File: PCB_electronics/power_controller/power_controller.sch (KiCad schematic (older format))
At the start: 20 parts, among them IC1 ATMEGA328-P, P1 SOLAR_PANEL, P2 5V_pololu, P3 BATT, P4 SUPERCAPS, P5 PWR_MEGA, P6 FEEDBACK_MEGA, U1 IRLB-8721_SOL, U2 IRLB-8721_MEGA, Y1 16MHz

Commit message: first version of power controller
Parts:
- IC1: footprint Housings_DIP:DIP-28_W15.24mm_LongPads -> Housings_DIP:DIP-28_W7.62mm_LongPads
- R1, R2, R3, R4, R5, R6, R7: footprint Resistors_ThroughHole:Resistor_Horizontal_RM20mm -> Resistors_ThroughHole:Resistor_Horizontal_RM10mm
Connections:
- net +5V: no longer IC1.21 (AREF)
- no-connect marks 14 -> 15

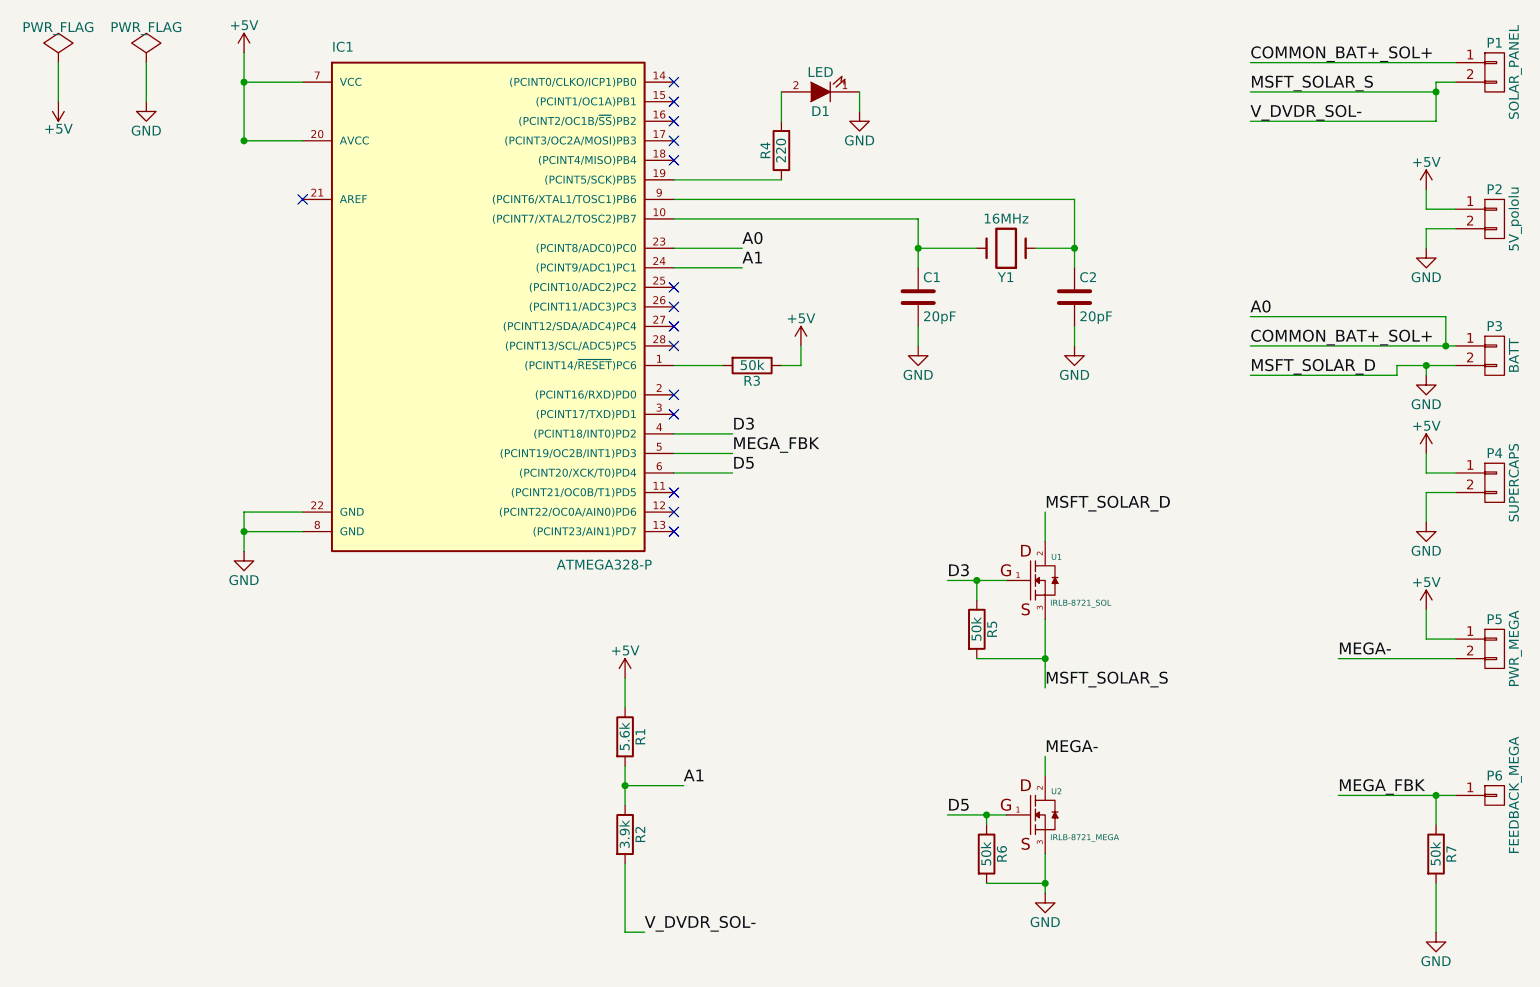
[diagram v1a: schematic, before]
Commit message: correct new PSB with net-tie on master
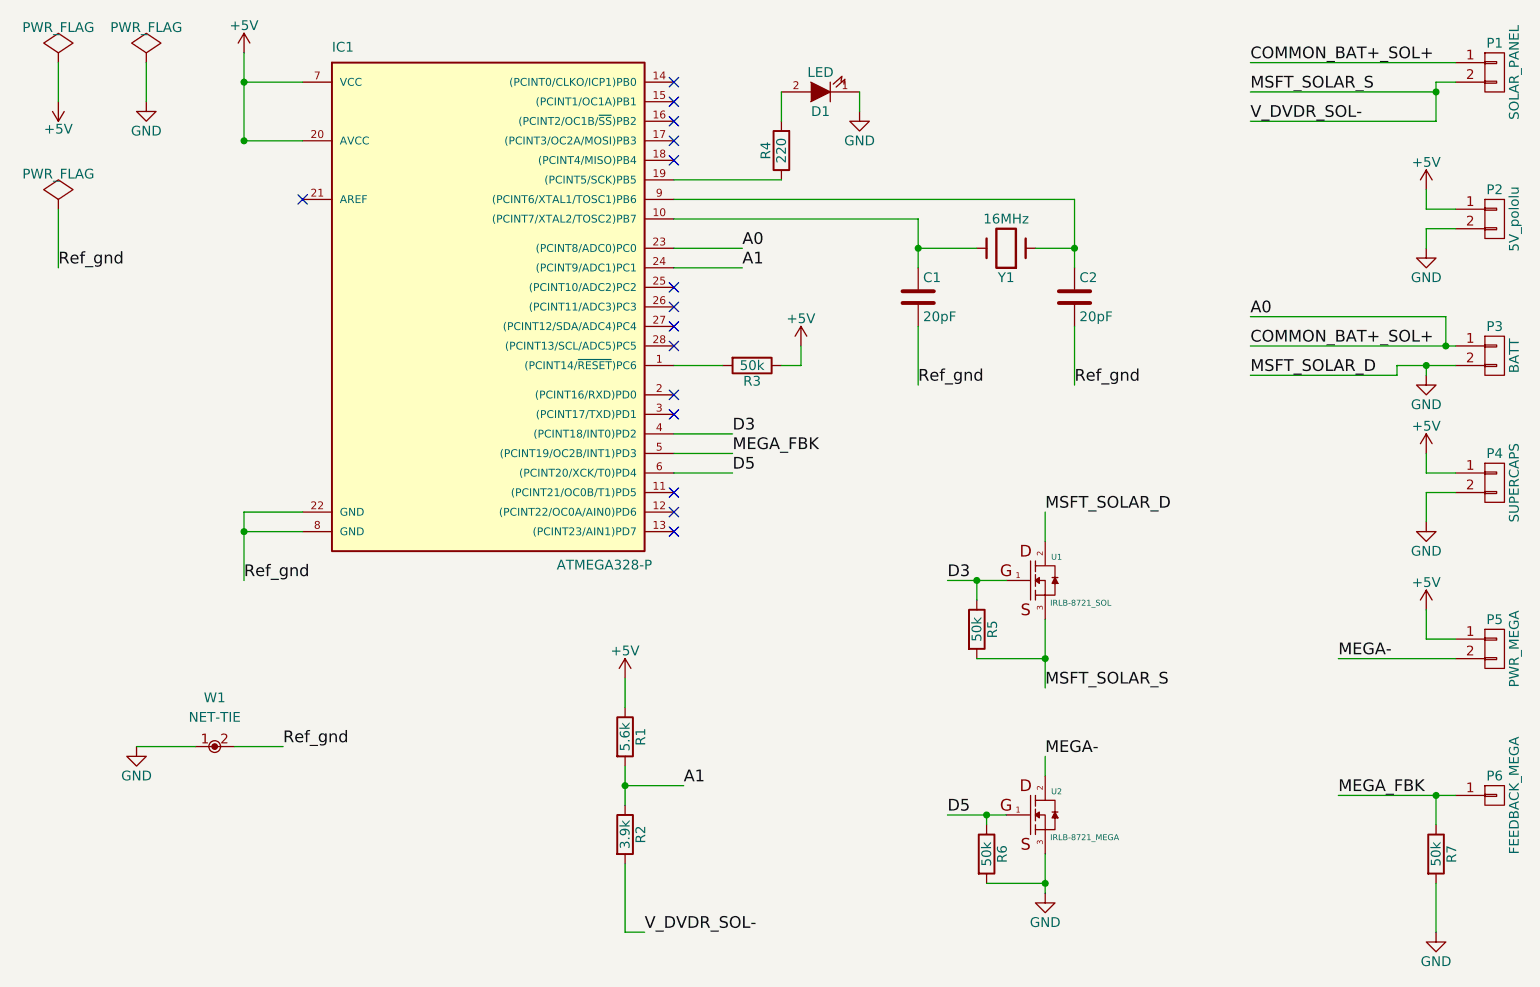
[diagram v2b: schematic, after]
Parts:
- added W1: NET-TIE, conn-test:NET-TIE, symbol NET-TIE
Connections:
- net GND: now also W1.1; no longer C1.2, C2.2, IC1.22 (GND), IC1.8 (GND)
- new net Ref_gnd: C1.2, C2.2, IC1.22 (GND), IC1.8 (GND), W1.2
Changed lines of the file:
@@
 LIBS:MOSFET-P
 LIBS:MOSFET-N
+LIBS:net-tie
 LIBS:power_controller-cache
 EELAYER 25 0
@@
 $EndComp
 $Comp
-L GND #PWR8
-U 1 1 5A1C2D72
-P 5200 3050
-F 0 "#PWR8" H 5200 2800 50  0001 C CNN
-F 1 "GND" H 5200 2900 50  0000 C CNN
-F 2 "" H 5200 3050 50  0000 C CNN
-F 3 "" H 5200 3050 50  0000 C CNN
-	1    5200 3050
-	1    0    0    -1
-$EndComp
-$Comp
-L GND #PWR10
-U 1 1 5A1C2D8E
-P 6000 3050
-F 0 "#PWR10" H 6000 2800 50  0001 C CNN
-F 1 "GND" H 6000 2900 50  0000 C CNN
-F 2 "" H 6000 3050 50  0000 C CNN
-F 3 "" H 6000 3050 50  0000 C CNN
-	1    6000 3050
-	1    0    0    -1
-$EndComp
-$Comp
-L GND #PWR4
-U 1 1 5A1C2E28
-P 1750 4100
-F 0 "#PWR4" H 1750 3850 50  0001 C CNN
-F 1 "GND" H 1750 3950 50  0000 C CNN
-F 2 "" H 1750 4100 50  0000 C CNN
-F 3 "" H 1750 4100 50  0000 C CNN
-	1    1750 4100
-	1    0    0    -1
-$EndComp
-$Comp
-L +5V #PWR3
+L +5V #PWR01
 U 1 1 5A1C2ED1
 P 1750 1550
-F 0 "#PWR3" H 1750 1400 50  0001 C CNN
+F 0 "#PWR01" H 1750 1400 50  0001 C CNN
 F 1 "+5V" H 1750 1690 50  0000 C CNN
 F 2 "" H 1750 1550 50  0000 C CNN
@@
 $EndComp
 $Comp
-L GND #PWR12
+L GND #PWR02
 U 1 1 5A1C31B8
 P 7800 2550
-F 0 "#PWR12" H 7800 2300 50  0001 C CNN
+F 0 "#PWR02" H 7800 2300 50  0001 C CNN
 F 1 "GND" H 7800 2400 50  0000 C CNN
 F 2 "" H 7800 2550 50  0000 C CNN
@@
 $EndComp
 $Comp
-L +5V #PWR11
+L +5V #PWR03
 U 1 1 5A1C322F
 P 7800 2250
-F 0 "#PWR11" H 7800 2100 50  0001 C CNN
+F 0 "#PWR03" H 7800 2100 50  0001 C CNN
 F 1 "+5V" H 7800 2390 50  0000 C CNN
 F 2 "" H 7800 2250 50  0000 C CNN
@@
 $EndComp
 $Comp
-L +5V #PWR14
+L +5V #PWR04
 U 1 1 5A1C3274
 P 7800 3600
-F 0 "#PWR14" H 7800 3450 50  0001 C CNN
+F 0 "#PWR04" H 7800 3450 50  0001 C CNN
 F 1 "+5V" H 7800 3740 50  0000 C CNN
 F 2 "" H 7800 3600 50  0000 C CNN
@@
 $EndComp
 $Comp
-L GND #PWR15
+L GND #PWR05
 U 1 1 5A1C3298
 P 7800 3950
-F 0 "#PWR15" H 7800 3700 50  0001 C CNN
+F 0 "#PWR05" H 7800 3700 50  0001 C CNN
 F 1 "GND" H 7800 3800 50  0000 C CNN
 F 2 "" H 7800 3950 50  0000 C CNN
@@
 A0
 $Comp
-L GND #PWR13
+L GND #PWR06
 U 1 1 5A1C3813
 P 7800 3200
-F 0 "#PWR13" H 7800 2950 50  0001 C CNN
+F 0 "#PWR06" H 7800 2950 50  0001 C CNN
 F 1 "GND" H 7800 3050 50  0000 C CNN
 F 2 "" H 7800 3200 50  0000 C CNN
@@
 $EndComp
 $Comp
-L +5V #PWR6
+L +5V #PWR07
 U 1 1 5A1C3B75
 P 4600 3050
-F 0 "#PWR6" H 4600 2900 50  0001 C CNN
+F 0 "#PWR07" H 4600 2900 50  0001 C CNN
 F 1 "+5V" H 4600 3190 50  0000 C CNN
 F 2 "" H 4600 3050 50  0000 C CNN
@@
 $EndComp
 $Comp
-L +5V #PWR16
+L +5V #PWR08
 U 1 1 5A1C4CA7
 P 7800 4400
-F 0 "#PWR16" H 7800 4250 50  0001 C CNN
+F 0 "#PWR08" H 7800 4250 50  0001 C CNN
 F 1 "+5V" H 7800 4540 50  0000 C CNN
 F 2 "" H 7800 4400 50  0000 C CNN
@@
 D5
 $Comp
-L GND #PWR9
+L GND #PWR09
 U 1 1 5A1C4F56
 P 5850 5850
-F 0 "#PWR9" H 5850 5600 50  0001 C CNN
+F 0 "#PWR09" H 5850 5600 50  0001 C CNN
 F 1 "GND" H 5850 5700 50  0000 C CNN
 F 2 "" H 5850 5850 50  0000 C CNN
@@
 $EndComp
 $Comp
-L GND #PWR17
+L GND #PWR010
 U 1 1 5A1C53D1
 P 7850 6050
-F 0 "#PWR17" H 7850 5800 50  0001 C CNN
+F 0 "#PWR010" H 7850 5800 50  0001 C CNN
 F 1 "GND" H 7850 5900 50  0000 C CNN
 F 2 "" H 7850 6050 50  0000 C CNN
@@
 $EndComp
 $Comp
-L +5V #PWR5
+L +5V #PWR011
 U 1 1 5A1C56C1
 P 3700 4750
-F 0 "#PWR5" H 3700 4600 50  0001 C CNN
+F 0 "#PWR011" H 3700 4600 50  0001 C CNN
 F 1 "+5V" H 3700 4890 50  0000 C CNN
 F 2 "" H 3700 4750 50  0000 C CNN
@@
 $EndComp
 $Comp
-L GND #PWR7
+L GND #PWR012
 U 1 1 5A1C6279
 P 4900 1850
-F 0 "#PWR7" H 4900 1600 50  0001 C CNN
+F 0 "#PWR012" H 4900 1600 50  0001 C CNN
 F 1 "GND" H 4900 1700 50  0000 C CNN
 F 2 "" H 4900 1850 50  0000 C CNN
@@
 NoConn ~ 3950 1700
 $Comp
-L PWR_FLAG #FLG2
+L PWR_FLAG #FLG013
 U 1 1 5A1C6663
 P 1250 1600
-F 0 "#FLG2" H 1250 1695 50  0001 C CNN
+F 0 "#FLG013" H 1250 1695 50  0001 C CNN
 F 1 "PWR_FLAG" H 1250 1780 50  0000 C CNN
 F 2 "" H 1250 1600 50  0000 C CNN
@@
 $EndComp
 $Comp
-L PWR_FLAG #FLG1
+L PWR_FLAG #FLG014
 U 1 1 5A1C66B3
 P 800 1600
-F 0 "#FLG1" H 800 1695 50  0001 C CNN
+F 0 "#FLG014" H 800 1695 50  0001 C CNN
 F 1 "PWR_FLAG" H 800 1780 50  0000 C CNN
 F 2 "" H 800 1600 50  0000 C CNN
@@
 $EndComp
 $Comp
-L +5V #PWR1
+L +5V #PWR015
 U 1 1 5A1C66EF
 P 800 1800
-F 0 "#PWR1" H 800 1650 50  0001 C CNN
+F 0 "#PWR015" H 800 1650 50  0001 C CNN
 F 1 "+5V" H 800 1940 50  0000 C CNN
 F 2 "" H 800 1800 50  0000 C CNN
@@
 $EndComp
 $Comp
-L GND #PWR2
+L GND #PWR016
 U 1 1 5A1C672B
 P 1250 1800
-F 0 "#PWR2" H 1250 1550 50  0001 C CNN
+F 0 "#PWR016" H 1250 1550 50  0001 C CNN
 F 1 "GND" H 1250 1650 50  0000 C CNN
 F 2 "" H 1250 1800 50  0000 C CNN
@@
 	3950 2300 6000 2300
 Wire Wire Line
-	5200 2950 5200 3050
-Wire Wire Line
-	6000 2950 6000 3050
+	5200 2950 5200 3250
+Wire Wire Line
+	6000 2950 6000 3250
 Wire Wire Line
 	1750 1700 2050 1700
@@
 Connection ~ 1750 2000
 Wire Wire Line
-	1750 3900 1750 4100
+	1750 3900 1750 4250
 Wire Wire Line
 	1750 4000 2050 4000
@@
 Wire Wire Line
 	1750 2000 1750 1550
+Text Label 5200 3250 0    60   ~ 0
+Ref_gnd
+Text Label 6000 3250 0    60   ~ 0
+Ref_gnd
+Text Label 1750 4250 0    60   ~ 0
+Ref_gnd
+Text Label 800  2650 0    60   ~ 0
+Ref_gnd
+$Comp
+L PWR_FLAG #FLG017
+U 1 1 5A1DC4FC
+P 800 2350
+F 0 "#FLG017" H 800 2445 50  0001 C CNN
+F 1 "PWR_FLAG" H 800 2530 50  0000 C CNN
+F 2 "" H 800 2350 50  0000 C CNN
+F 3 "" H 800 2350 50  0000 C CNN
+	1    800  2350
+	1    0    0    -1
+$EndComp
+Wire Wire Line
+	800  2350 800  2650
+$Comp
+L NET-TIE W1
+U 1 1 5A1DD135
+P 1600 5100
+F 0 "W1" H 1600 5350 50  0000 C CNN
+F 1 "NET-TIE" H 1600 5250 50  0000 C CNN
+F 2 "conn-test:NET-TIE" H 1600 5000 50  0001 C CNN
+F 3 "" H 1600 5100 60  0000 C CNN
+	1    1600 5100
+	1    0    0    -1
+$EndComp
+Text Label 1950 5100 0    60   ~ 0
+Ref_gnd
+Wire Wire Line
+	1700 5100 1950 5100
+$Comp
+L GND #PWR018
+U 1 1 5A1DD272
+P 1200 5100
+F 0 "#PWR018" H 1200 4850 50  0001 C CNN
+F 1 "GND" H 1200 4950 50  0000 C CNN
+F 2 "" H 1200 5100 50  0000 C CNN
+F 3 "" H 1200 5100 50  0000 C CNN
+	1    1200 5100
+	1    0    0    -1
+$EndComp
+Wire Wire Line
+	1200 5100 1500 5100
 $EndSCHEMATC

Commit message: files to send to Olav for double checking
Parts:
- U1: value IRLB-8721_SOL -> IRLB_8721_SOL
- U2: value IRLB-8721_MEGA -> IRLS-8721_MEGA
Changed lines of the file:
@@
 LIBS:MOSFET-N
 LIBS:net-tie
+LIBS:my_mosfet-n
 LIBS:power_controller-cache
 EELAYER 25 0
@@
 	1    0    0    -1
 $EndComp
-$Comp
-L MOSFET-N U1
-U 1 1 5A1C3CAA
-P 5850 4250
-F 0 "U1" H 5880 4370 30  0000 L CNN
-F 1 "IRLB-8721_SOL" H 5875 4135 30  0000 L CNN
-F 2 "TO_SOT_Packages_THT:TO-220_Neutral123_Vertical" H 5850 4200 60  0001 C CNN
-F 3 "" H 5850 4200 60  0000 C CNN
-	1    5850 4250
-	1    0    0    -1
-$EndComp
 Text Label 5850 3900 0    60   ~ 0
 MSFT_SOLAR_D
@@
 F 3 "" H 5500 4500 50  0000 C CNN
 	1    5500 4500
-	1    0    0    -1
-$EndComp
-$Comp
-L MOSFET-N U2
-U 1 1 5A1C4C0F
-P 5850 5450
-F 0 "U2" H 5880 5570 30  0000 L CNN
-F 1 "IRLB-8721_MEGA" H 5875 5335 30  0000 L CNN
-F 2 "TO_SOT_Packages_THT:TO-220_Neutral123_Vertical" H 5850 5400 60  0001 C CNN
-F 3 "" H 5850 5400 60  0000 C CNN
-	1    5850 5450
 	1    0    0    -1
 $EndComp
@@
 Wire Wire Line
 	1200 5100 1500 5100
+$Comp
+L MOSFET-N U1
+U 1 1 5A1EC6D2
+P 5850 4250
+F 0 "U1" H 5880 4370 30  0000 L CNN
+F 1 "IRLB_8721_SOL" H 5875 4135 30  0000 L CNN
+F 2 "TO_SOT_Packages_THT:TO-220_Neutral123_Vertical" H 5850 4200 60  0001 C CNN
+F 3 "" H 5850 4200 60  0000 C CNN
+	1    5850 4250
+	1    0    0    -1
+$EndComp
+$Comp
+L MOSFET-N U2
+U 1 1 5A1EC71D
+P 5850 5450
+F 0 "U2" H 5880 5570 30  0000 L CNN
+F 1 "IRLS-8721_MEGA" H 5875 5335 30  0000 L CNN
+F 2 "TO_SOT_Packages_THT:TO-220_Neutral123_Vertical" H 5850 5400 60  0001 C CNN
+F 3 "" H 5850 5400 60  0000 C CNN
+	1    5850 5450
+	1    0    0    -1
+$EndComp
 $EndSCHEMATC
